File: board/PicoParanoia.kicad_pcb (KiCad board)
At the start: 2 copper layers, 84 x 92 mm, 61 parts, among them J1 RCAJack, J2 Barrel_Jack_Switch, J3 Conn_01x04_Pin, J4 DE9_Plug, P1 Mini-DIN_6pins_ver4, Q1 2N3904, Q2 2N3904, Q3 2N3904, Q4 2N3904, U1 MicroSD_SPI_CD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

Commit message: JLCPCB order
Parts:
- added C16: 100 nF, Capacitor_THT:C_Disc_D5.0mm_W2.5mm_P5.00mm, F.Cu at (71.6, 57.4)
- H1, H2, H3, H4: value MountingHole -> MountingHole_Pad; footprint MountingHole:MountingHole_3.2mm_M3 -> MountingHole:MountingHole_3.2mm_M3_Pad
- moved H2 84.0 mm to (145.0, 51.0)
- moved H3 84.0 mm to (69.0, 135.0)
- moved H1 76.0 mm to (69.0, 51.0)
- moved H4 76.0 mm to (145.0, 135.0)
- moved D3 2.89 mm to (101.3, 59.7)
- moved Q2 1.61 mm to (97.7, 52.0)
- moved L1 1.02 mm to (90.7, 56.1)
- moved Q1 0.55 mm to (95.5, 51.4)
- moved R14 0.26 mm to (87.8, 59.5)
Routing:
- net GND: track 515.6 -> 629.4 mm, vias 130 -> 159
- net +5V: track 218.3 -> 225.1 mm
- net Net-(D3-K): track 50.6 -> 53.6 mm
- net Net-(D3-A): track 13.6 -> 15.5 mm
- net Net-(Q2-B): track 38.9 -> 37.4 mm
- net +3.3V: track 110.7 -> 110.1 mm
- net /CTS: track 65.5 -> 64.9 mm
- net Net-(Q1-B): track 41.2 -> 41.7 mm
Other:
- board text added: "SERIAL PORT (DTE)"
- board text removed: "SERIAL PORT"

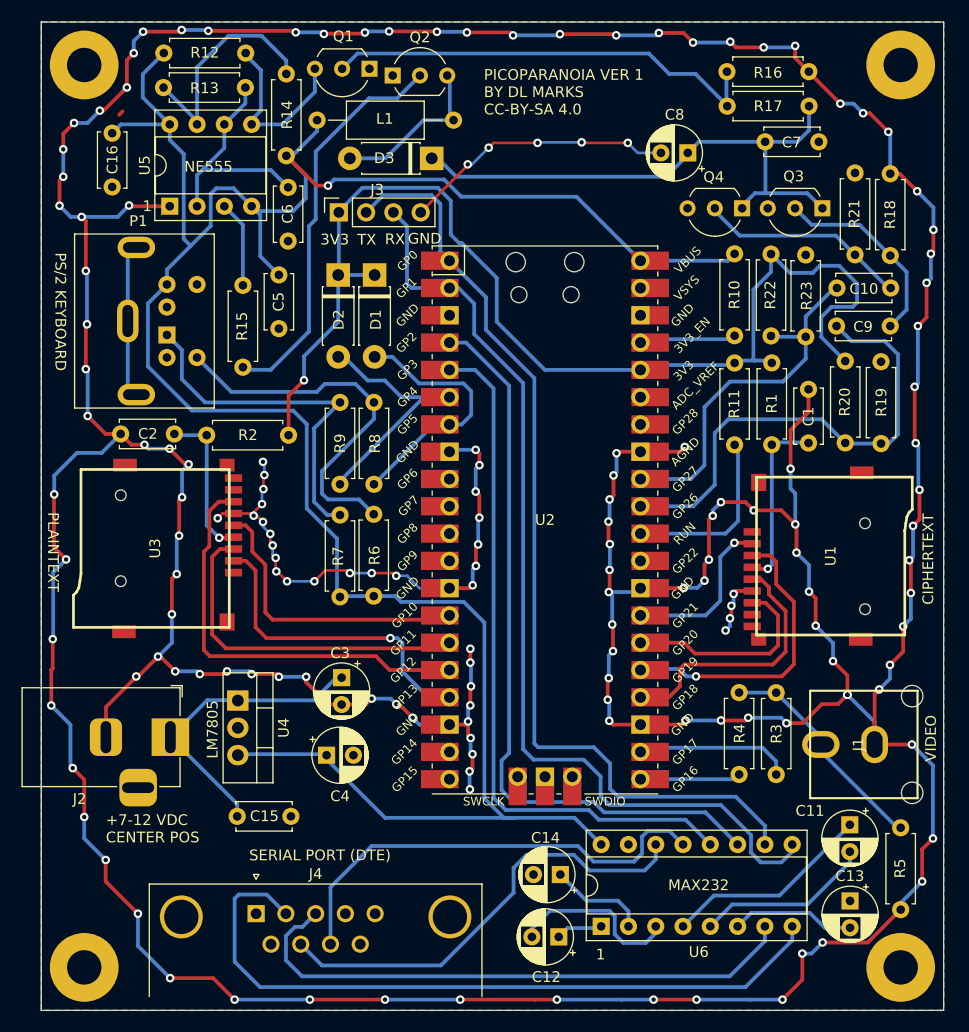
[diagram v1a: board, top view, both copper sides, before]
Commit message: Swapped cipher and plaintext cards
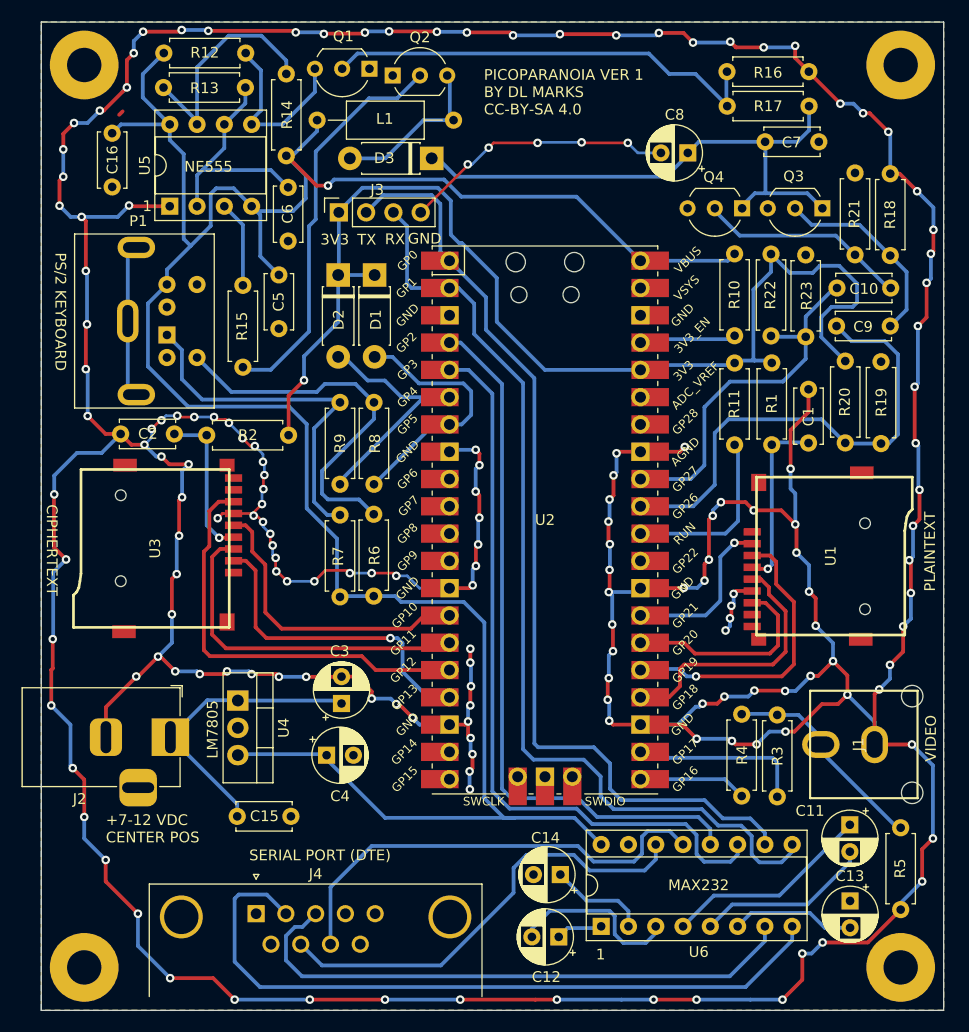
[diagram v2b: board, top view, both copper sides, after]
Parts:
- moved C3 2.41 mm to (93.0, 110.4), turned to 90 degrees
- moved R3 2.07 mm to (133.5, 119.1)
- moved R4 2.02 mm to (130.2, 119.0)
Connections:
- U2 pad 4: /RTS -> /CTS
- U2 pad 5: /CTS -> /RTS
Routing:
- net GND: track 629.4 -> 666.0 mm, vias 159 -> 171
- net /PICTURE: track 14.5 -> 16.3 mm
- net /CTS: track 64.9 -> 66.6 mm
- net Net-(J1-PIN): track 21.0 -> 20.0 mm
- net Net-(U4-VI): track 28.2 -> 27.4 mm
- net /VSYNC: track 9.36 -> 10.1 mm
- net /SCK2: track 27.6 -> 28.3 mm
- net /RTS: track 69.2 -> 69.7 mm
